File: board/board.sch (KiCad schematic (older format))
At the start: 9 parts, among them IC1 ATMEGA328-P, P1 CONN_02X03, P2 CONN_01X04, SW1 RESET, U1 ILI9341_LCD_Breakout, Y1 Crystal

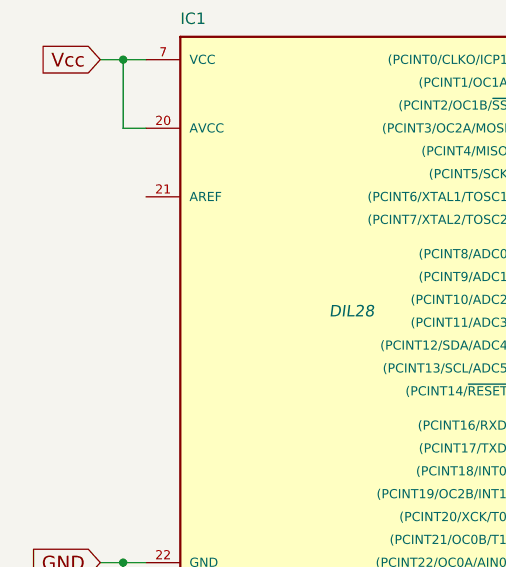
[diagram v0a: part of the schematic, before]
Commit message: Added capacitor to aref pin and updated sheet info
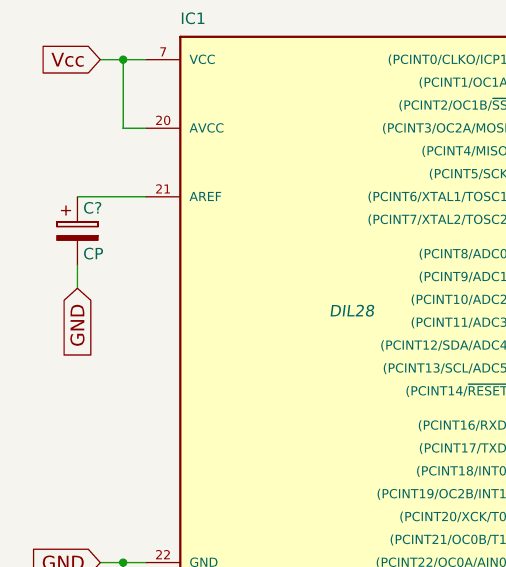
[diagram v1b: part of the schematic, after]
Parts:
- added C?: CP, symbol CP
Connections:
- net GND: now also C?.2
- net at IC1.21 (AREF): now also C?.1
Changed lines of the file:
@@
 encoding utf-8
 Sheet 1 1
-Title ""
+Title "SerialMonitor"
 Date ""
-Rev ""
-Comp ""
+Rev "0.1"
+Comp "DrMaker"
 Comment1 ""
 Comment2 ""
@@
 Wire Wire Line
 	4050 4500 3900 4500
+$Comp
+L CP C?
+U 1 1 573F26E6
+P 1100 2000
+F 0 "C?" H 1125 2100 50  0000 L CNN
+F 1 "CP" H 1125 1900 50  0000 L CNN
+F 2 "" H 1138 1850 50  0000 C CNN
+F 3 "" H 1100 2000 50  0000 C CNN
+	1    1100 2000
+	1    0    0    -1
+$EndComp
+Wire Wire Line
+	1400 1850 1100 1850
+Text GLabel 1100 2250 3    60   Input ~ 0
+GND
+Wire Wire Line
+	1100 2250 1100 2150
 $EndSCHEMATC

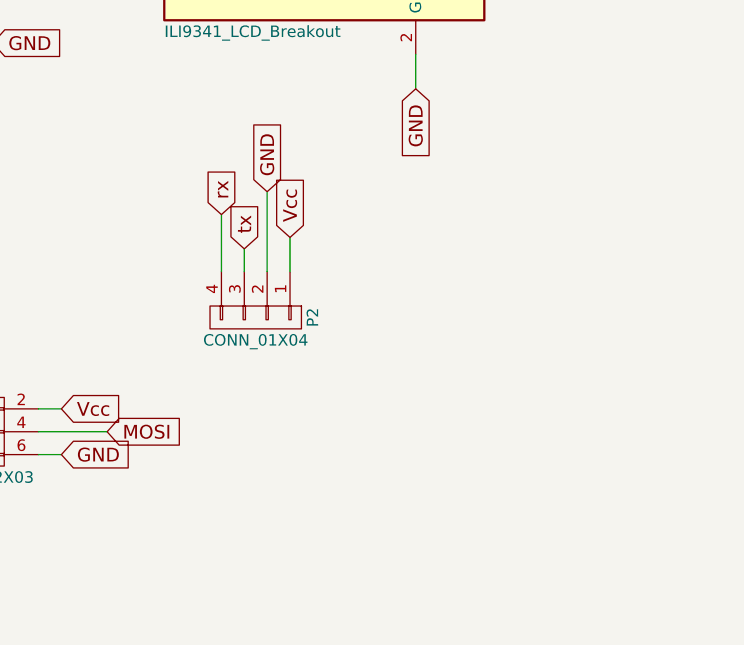
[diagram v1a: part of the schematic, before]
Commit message: added spdt switch to turn on/off the device
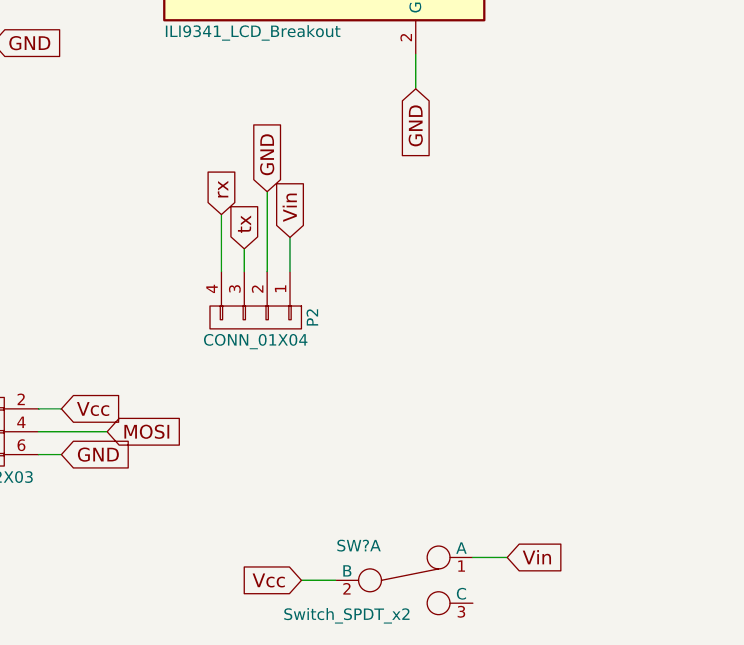
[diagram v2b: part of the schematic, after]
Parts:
- added SW?: Switch_SPDT_x2, symbol Switch_SPDT_x2
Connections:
- net Vcc: now also SW?.2 (B); no longer P2.1 (P1)
- new net Vin: P2.1 (P1), SW?.1 (A)
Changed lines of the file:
@@
 $EndComp
 Text GLabel 5650 3550 1    60   Input ~ 0
-Vcc
+Vin
 Wire Wire Line
 	5650 3550 5650 3700
@@
 Wire Wire Line
 	1100 2250 1100 2150
+$Comp
+L Switch_SPDT_x2 SW?
+U 1 1 573F3661
+P 6150 5050
+F 0 "SW?" H 5950 5200 50  0000 C CNN
+F 1 "Switch_SPDT_x2" H 5900 4900 50  0000 C CNN
+F 2 "" H 6150 5050 50  0000 C CNN
+F 3 "" H 6150 5050 50  0000 C CNN
+	1    6150 5050
+	1    0    0    -1
+$EndComp
+Text GLabel 5700 5050 0    60   Input ~ 0
+Vcc
+Wire Wire Line
+	5700 5050 5850 5050
+Text GLabel 6600 4950 2    60   Input ~ 0
+Vin
+Wire Wire Line
+	6600 4950 6450 4950
 $EndSCHEMATC
